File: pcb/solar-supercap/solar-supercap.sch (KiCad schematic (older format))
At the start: 6 parts, among them P1 SOLAR, P2 OUT

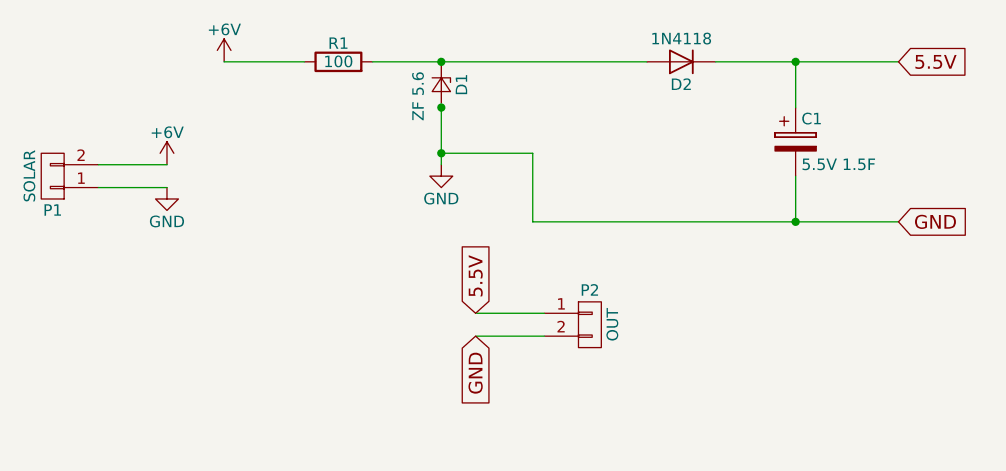
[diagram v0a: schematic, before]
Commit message: added 51k/10k for solar power to atmel
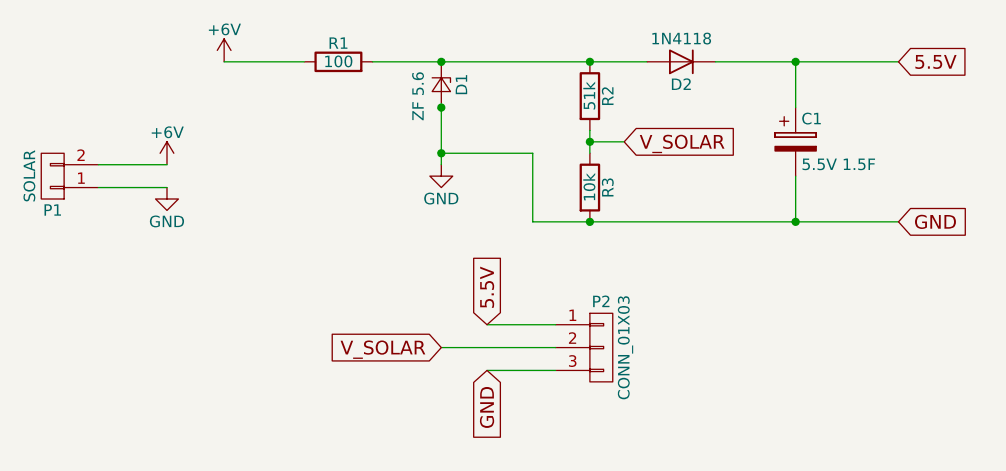
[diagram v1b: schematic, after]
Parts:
- removed P2: OUT, symbol CONN_01X02
- added P2: CONN_01X03, symbol CONN_01X03
- added R2: 51k, symbol R
- added R3: 10k, symbol R
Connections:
- net 5.5V: now also P2.1 (P1)
- net GND: now also P2.3 (P3), R3.2
- net at D1.1 (K), D2.2 (A), R1.2: now also R2.1
- new net V_SOLAR: P2.2 (P2), R2.2, R3.1
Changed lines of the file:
@@
 LIBS:contrib
 LIBS:valves
+LIBS:solar-supercap-cache
 EELAYER 25 0
 EELAYER END
@@
 Text GLabel 5500 1950 2    60   Input ~ 0
 GND
-Text GLabel 3650 2350 1    60   Input ~ 0
+Text GLabel 3700 2400 1    60   Input ~ 0
 5.5V
-Text GLabel 3650 2450 3    60   Input ~ 0
+Text GLabel 3700 2600 3    60   Input ~ 0
 GND
-$Comp
-L CONN_01X02 P2
-U 1 1 599B19F6
-P 4150 2400
-F 0 "P2" H 4150 2550 50  0000 C CNN
-F 1 "OUT" V 4250 2400 50  0000 C CNN
-F 2 "" H 4150 2400 50  0000 C CNN
-F 3 "" H 4150 2400 50  0000 C CNN
-	1    4150 2400
-	1    0    0    -1
-$EndComp
 Wire Wire Line
 	2300 1700 2000 1700
@@
 	4700 1250 5500 1250
 Wire Wire Line
-	3650 2350 3950 2350
-Wire Wire Line
-	3650 2450 3950 2450
-Wire Wire Line
 	5050 1450 5050 1250
 Connection ~ 5050 1250
@@
 	5050 1750 5050 1950
 Connection ~ 5050 1950
+$Comp
+L R R2
+U 1 1 59B1A4AE
+P 4150 1400
+F 0 "R2" V 4230 1400 50  0000 C CNN
+F 1 "51k" V 4150 1400 50  0000 C CNN
+F 2 "" V 4080 1400 50  0000 C CNN
+F 3 "" H 4150 1400 50  0000 C CNN
+	1    4150 1400
+	1    0    0    -1
+$EndComp
+$Comp
+L R R3
+U 1 1 59B1A4EC
+P 4150 1800
+F 0 "R3" V 4230 1800 50  0000 C CNN
+F 1 "10k" V 4150 1800 50  0000 C CNN
+F 2 "" V 4080 1800 50  0000 C CNN
+F 3 "" H 4150 1800 50  0000 C CNN
+	1    4150 1800
+	1    0    0    -1
+$EndComp
+Connection ~ 4150 1950
+Connection ~ 4150 1250
+Connection ~ 4150 1600
+Wire Wire Line
+	4150 1550 4150 1650
+Text GLabel 4300 1600 2    60   Input ~ 0
+V_SOLAR
+Wire Wire Line
+	4300 1600 4150 1600
+$Comp
+L CONN_01X03 P2
+U 1 1 59B1A79D
+P 4200 2500
+F 0 "P2" H 4200 2700 50  0000 C CNN
+F 1 "CONN_01X03" V 4300 2500 50  0000 C CNN
+F 2 "" H 4200 2500 50  0000 C CNN
+F 3 "" H 4200 2500 50  0000 C CNN
+	1    4200 2500
+	1    0    0    -1
+$EndComp
+Text GLabel 3500 2500 0    60   Input ~ 0
+V_SOLAR
+Wire Wire Line
+	4000 2400 3700 2400
+Wire Wire Line
+	4000 2500 3500 2500
+Wire Wire Line
+	4000 2600 3700 2600
 $EndSCHEMATC
